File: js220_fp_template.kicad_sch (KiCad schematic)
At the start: 5 parts, among them J1 JS220

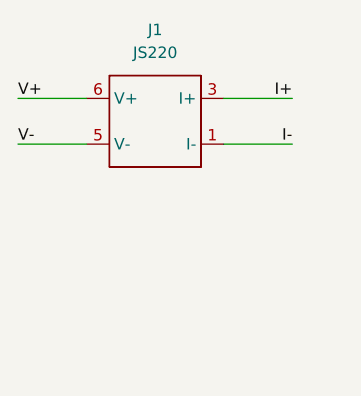
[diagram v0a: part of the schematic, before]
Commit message: Fixed flipped pinout with I+ I-
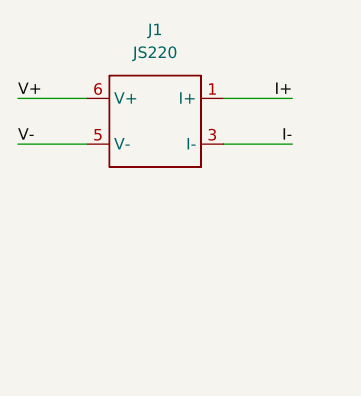
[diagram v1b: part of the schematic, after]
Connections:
- net I+: now also J1.1 (I+), J1.2 (I+); no longer J1.3 (I+), J1.4 (I+)
- net I-: now also J1.3 (I-), J1.4 (I-); no longer J1.1 (I-), J1.2 (I-)
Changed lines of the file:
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@@
   (title_block
     (title "Joulescope JS220 Front Panel Template")
-    (date "2022-10-23")
-    (rev "1.1")
+    (date "2022-11-12")
+    (rev "1.2")
     (company "Alvaro Prieto")
   )
@@
     (property "Reference" "J1" (id 0) (at 154.94 81.28 0))
     (property "Value" "JS220" (id 1) (at 154.94 83.82 0))
-    (property "Footprint" "Joulescope:SAMTEC_TSM-103-01-S-DV-A" (id 2) (at 154.94 93.98 0)
+    (property "Footprint" "Joulescope:SAMTEC_TSM-103-01-S-DV-A" (id 2) (at 154.94 99.06 0)
       (effects (font (size 1.27 1.27)) hide)
     )
